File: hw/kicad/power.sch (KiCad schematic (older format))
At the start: 56 parts

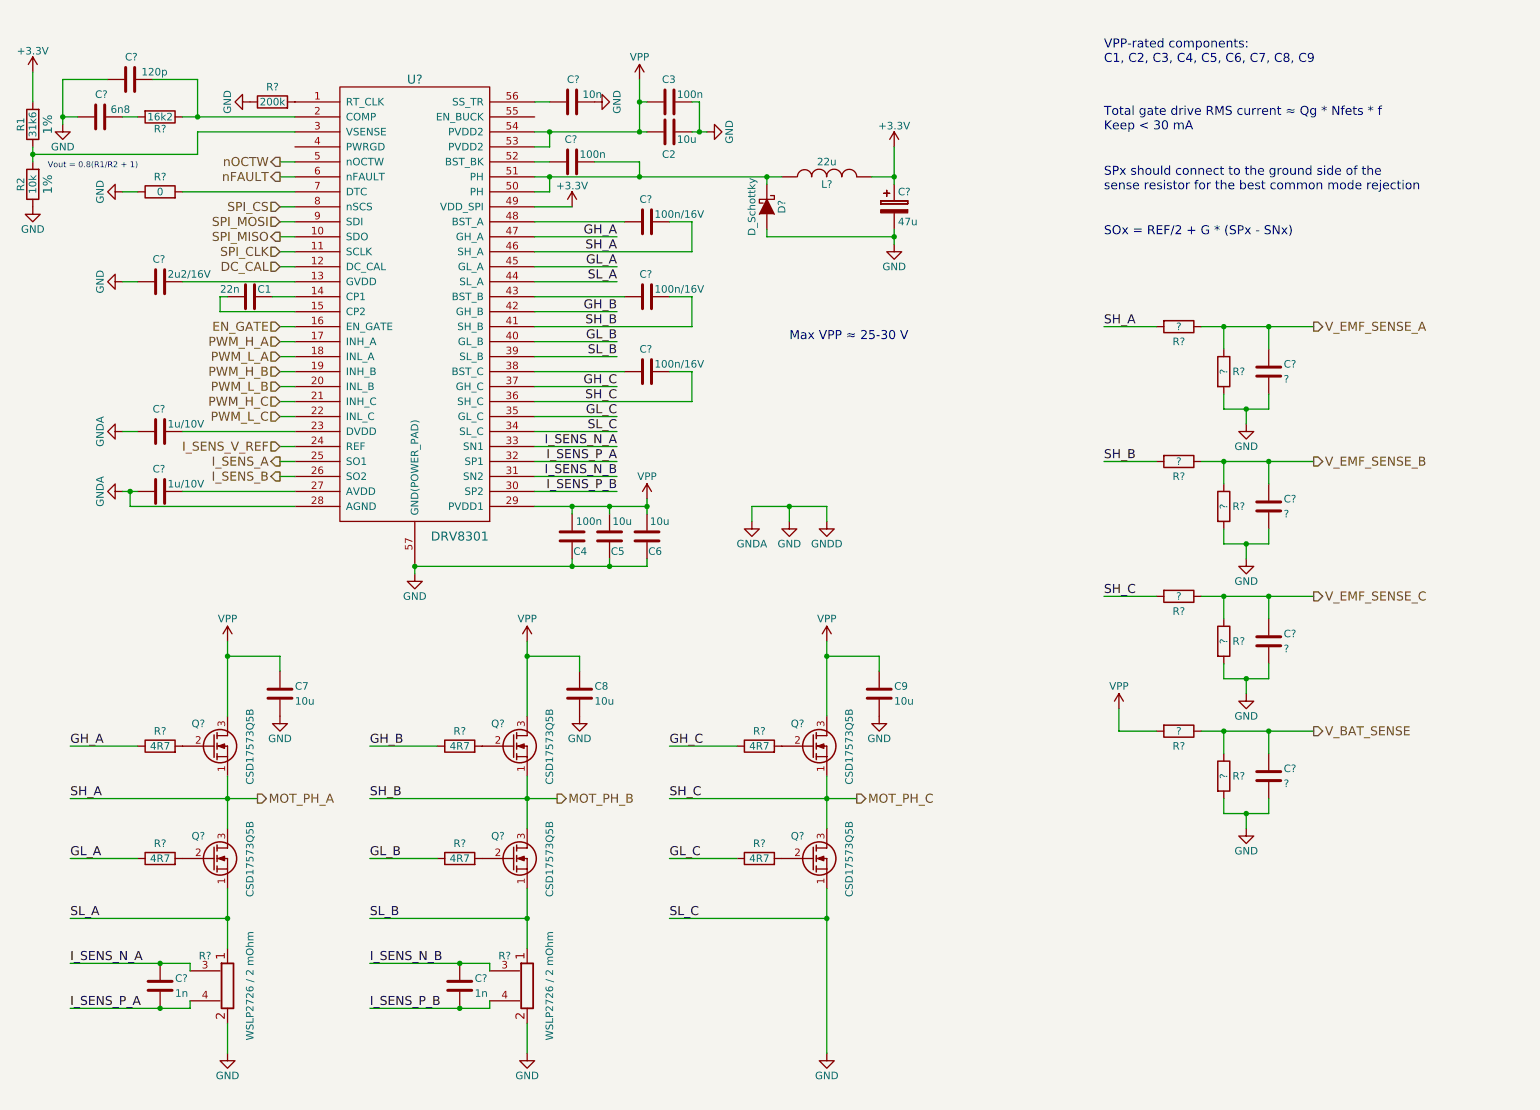
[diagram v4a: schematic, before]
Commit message: Connect mcu to drv8301
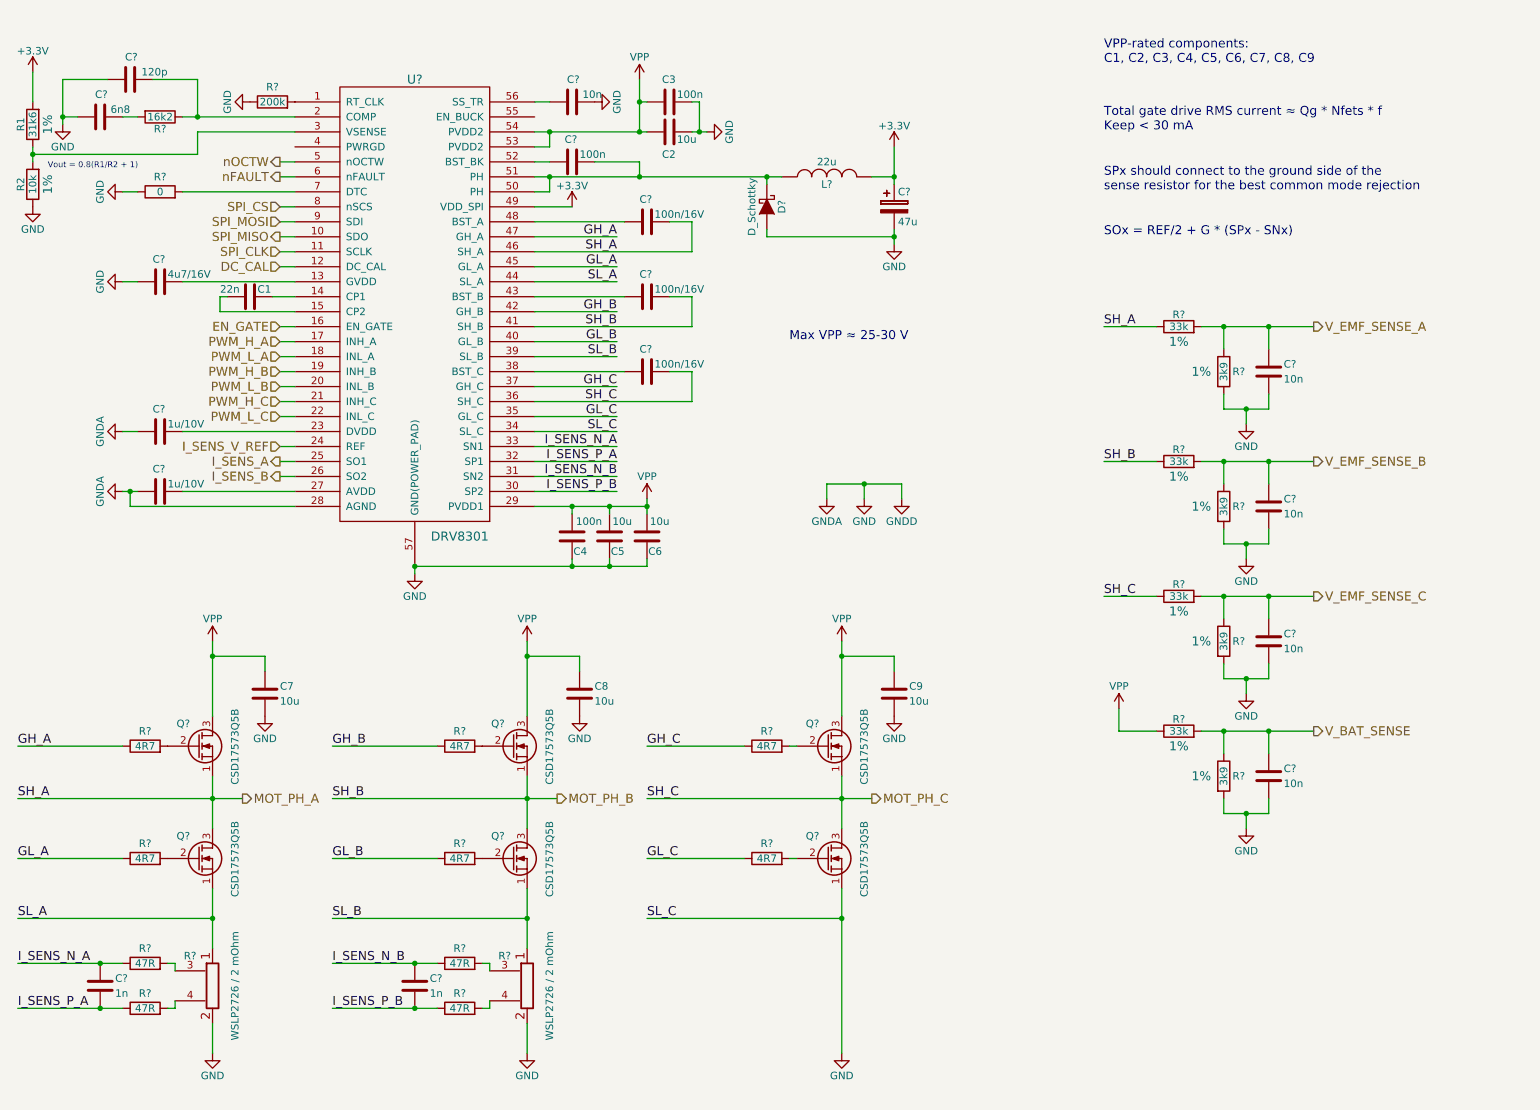
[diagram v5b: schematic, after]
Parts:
- removed C? (x3): ?, symbol C
- removed R? (x8): ?, symbol R
- removed R?: WSLP2726 / 2 mOhm, symbol WSLP2726
- added C? (x3): 10n, symbol C
- added R?: WSLP2726 / 2 mOhm, WSLP2726:WSLP2726, symbol WSLP2726
- added R? (x4): 33k, symbol R
- added R? (x4): 3k9, symbol R
- added R? (x4): 47R, symbol R
- C?: value 2u2/16V -> 4u7/16V
- C?: value ? -> 10n
- R?: footprint (none) -> WSLP2726:WSLP2726
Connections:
- net GND: now also C?.2, C?.2, C?.2, R?.2, R?.2, R?.2, R?.2, R?.2
- net I_SENS_N_A: now also R?.1; no longer R?.3
- net I_SENS_N_B: now also R?.1
- net I_SENS_P_A: now also R?.1; no longer R?.4
- net I_SENS_P_B: now also R?.1
- net MOT_PH_A: now also R?.1
- net MOT_PH_B: now also R?.1
- net MOT_PH_C: now also R?.1
- net SL_B: now also R?.1
- net VPP: now also R?.1
- net V_BAT_SENSE: now also C?.1, R?.1, R?.2
- net V_EMF_SENSE_A: now also R?.1, R?.2
- net V_EMF_SENSE_B: now also C?.1, R?.1, R?.2
- net V_EMF_SENSE_C: now also C?.1, R?.1, R?.2
- new net: R?.2, R?.3 (x2)
- new net: R?.2, R?.4 (x2)
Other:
- moved on the sheet: C7, C9, C?, Q?, R?

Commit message: Added LDO for mcu
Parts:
- R1: value 31k6 -> 36k
- R2: value 10k -> 6k8
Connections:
- net +3V3: no longer C?.1, L?.2, R1.2
- new net +5V: C?.1, L?.2, R1.2
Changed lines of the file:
@@
 LIBS:wslp2726
 LIBS:test
+LIBS:az1117c
 LIBS:MotCtrl-cache
 EELAYER 25 0
@@
 P 900 1650
 F 0 "R2" V 980 1650 50  0000 C CNN
-F 1 "10k" V 900 1650 50  0000 C CNN
+F 1 "6k8" V 900 1650 50  0000 C CNN
 F 2 "" V 830 1650 30  0000 C CNN
 F 3 "" H 900 1650 30  0000 C CNN
@@
 P 900 1250
 F 0 "R1" V 980 1250 50  0000 C CNN
-F 1 "31k6" V 900 1250 50  0000 C CNN
+F 1 "36k" V 900 1250 50  0000 C CNN
 F 2 "" V 830 1250 30  0000 C CNN
 F 3 "" H 900 1250 30  0000 C CNN
@@
 F 3 "" H 1100 1250 60  0000 C CNN
 	1    1100 1250
-	1    0    0    -1
-$EndComp
-$Comp
-L +3.3V #PWR?
-U 1 1 5815E769
-P 6650 1400
-F 0 "#PWR?" H 6650 1250 50  0001 C CNN
-F 1 "+3.3V" H 6650 1540 50  0000 C CNN
-F 2 "" H 6650 1400 60  0000 C CNN
-F 3 "" H 6650 1400 60  0000 C CNN
-	1    6650 1400
-	1    0    0    -1
-$EndComp
-$Comp
-L +3.3V #PWR?
-U 1 1 5815E7DD
-P 900 900
-F 0 "#PWR?" H 900 750 50  0001 C CNN
-F 1 "+3.3V" H 900 1040 50  0000 C CNN
-F 2 "" H 900 900 60  0000 C CNN
-F 3 "" H 900 900 60  0000 C CNN
-	1    900  900
 	1    0    0    -1
 $EndComp
@@
 	1    0    0    -1
 $EndComp
+$Comp
+L +5V #PWR?
+U 1 1 5823932E
+P 6650 1400
+F 0 "#PWR?" H 6650 1250 50  0001 C CNN
+F 1 "+5V" H 6650 1540 50  0000 C CNN
+F 2 "" H 6650 1400 60  0000 C CNN
+F 3 "" H 6650 1400 60  0000 C CNN
+	1    6650 1400
+	1    0    0    -1
+$EndComp
+$Comp
+L +5V #PWR?
+U 1 1 58239A98
+P 900 900
+F 0 "#PWR?" H 900 750 50  0001 C CNN
+F 1 "+5V" H 900 1040 50  0000 C CNN
+F 2 "" H 900 900 60  0000 C CNN
+F 3 "" H 900 900 60  0000 C CNN
+	1    900  900
+	1    0    0    -1
+$EndComp

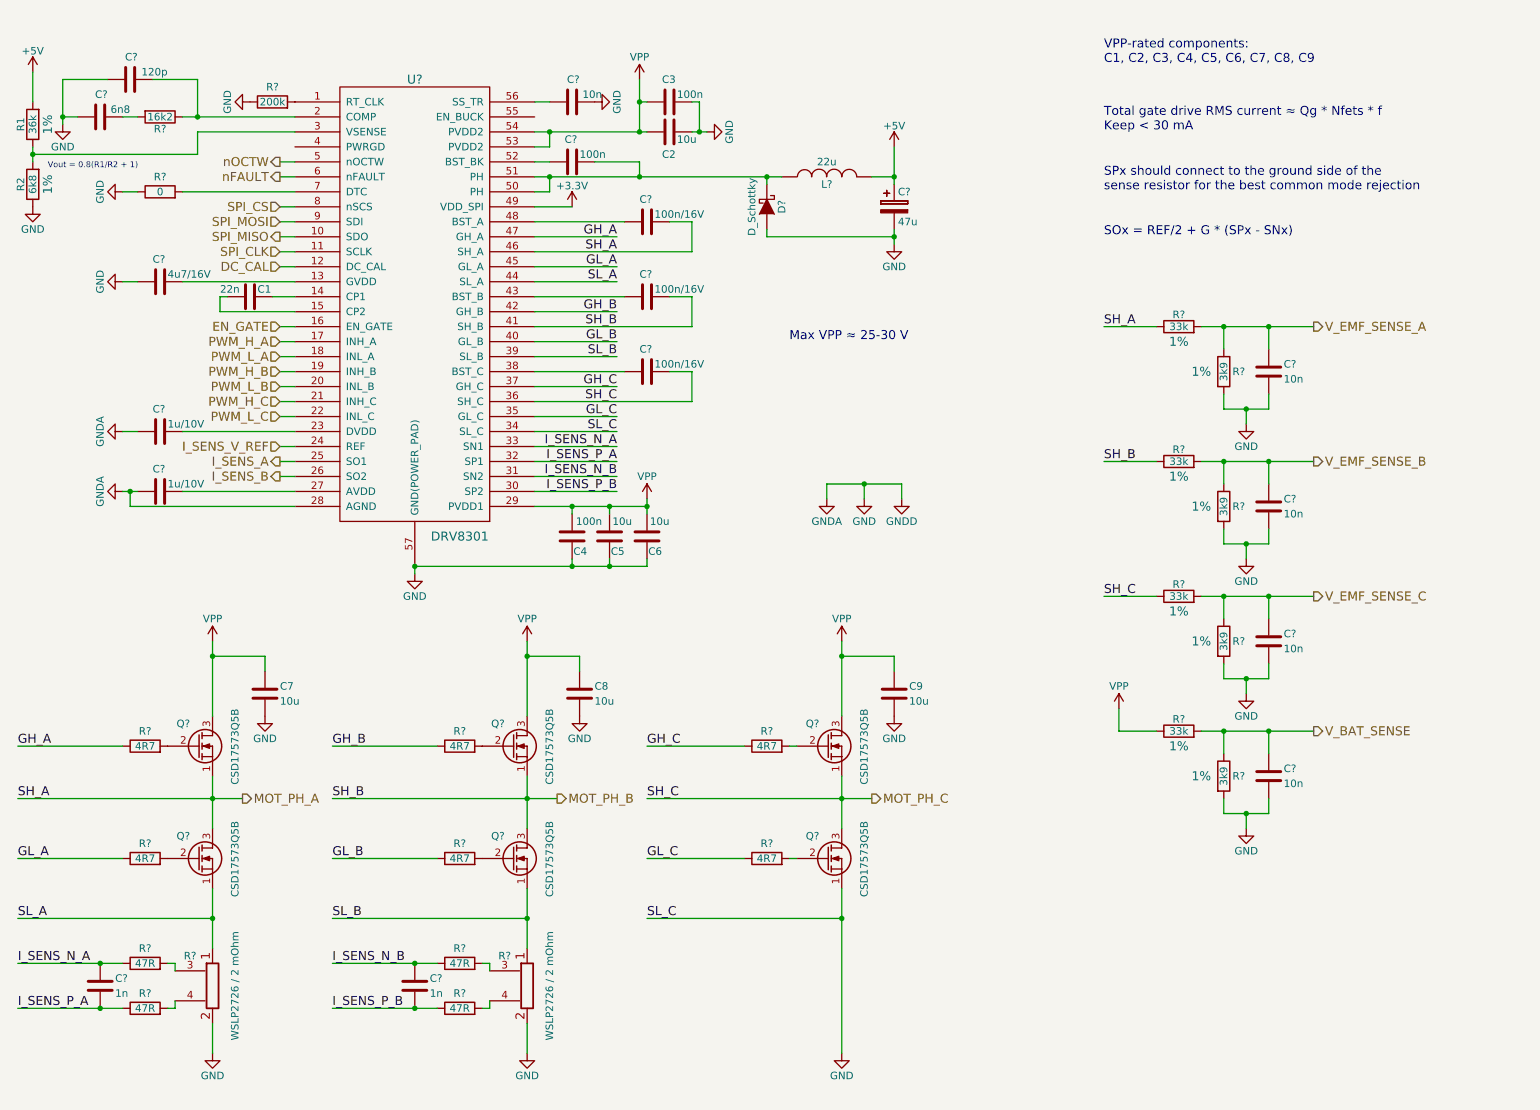
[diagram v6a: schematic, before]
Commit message: Big changes in power: new mosfets, drivers and current sensing
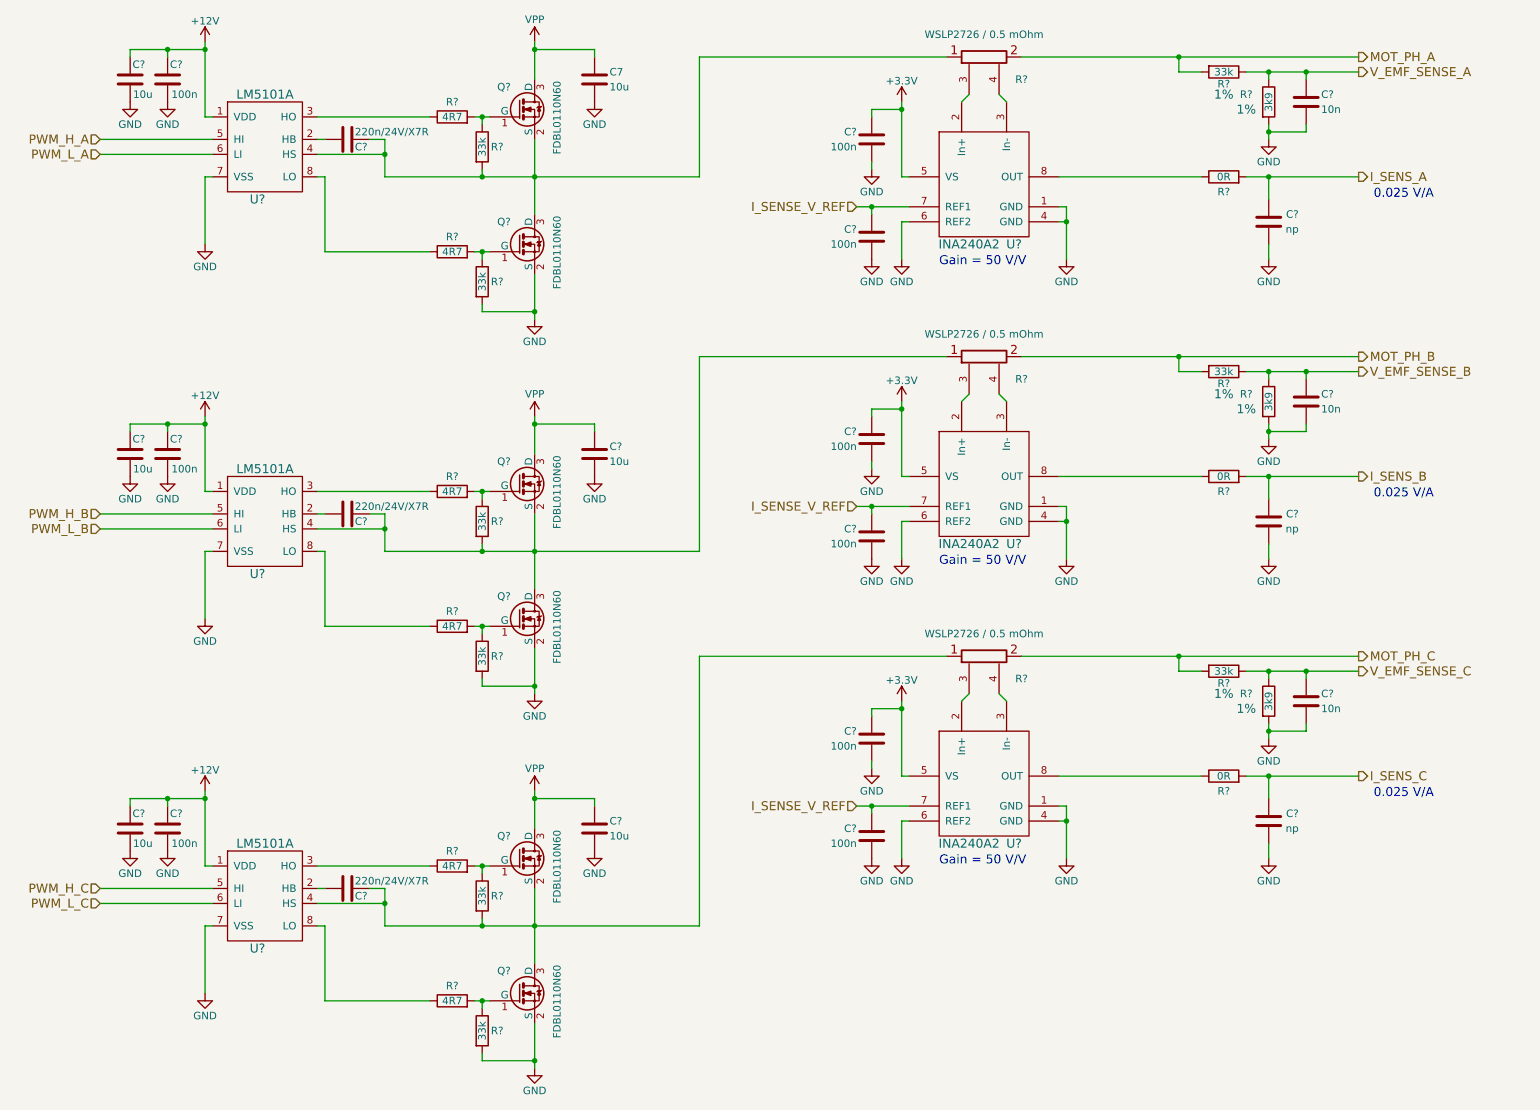
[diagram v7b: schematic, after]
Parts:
- removed C1: 22n, symbol C
- removed C2, C5, C6, C8, C9: 10u, symbol C
- removed C3, C4, C?: 100n, symbol C
- removed C? (x5): 10n, symbol C
- removed C?: 47u, symbol CP
- removed C?: 120p, symbol C
- removed C?: 6n8, symbol C
- removed C?: 4u7/16V, symbol C
- removed C? (x2): 1u/10V, symbol C
- removed C? (x3): 100n/16V, symbol C
- removed C? (x2): 1n, symbol C
- removed D?: D_Schottky, symbol D_Schottky
- removed L?: 22u, symbol INDUCTOR
- removed Q? (x6): CSD17573Q5B, SON_8_5x6:SON_8_5x6, symbol Q_NMOS_SGD
- removed R1: 36k, symbol R
- removed R2: 6k8, symbol R
- removed R?: 200k, symbol R
- removed R?: 16k2, symbol R
- removed R?: 0, symbol R
- removed R? (x4): 4R7, symbol R
- removed R?: WSLP2726 / 2 mOhm, WSLP2726:WSLP2726, symbol WSLP2726
- removed R? (x4): 33k, symbol R
- removed R? (x4): 3k9, symbol R
- removed R? (x4): 47R, symbol R
- removed U?: DRV8301, footprints:TSSOP-56-PP, symbol DRV8301
- added C? (x9): 100n, symbol C
- added C? (x3): np, symbol C
- added C? (x3): 10n, symbol C
- added C? (x3): 220n/24V/X7R, symbol C
- added C? (x5): 10u, symbol C
- added Q? (x6): FDBL0110N60, MO-299A:MO-299A, symbol FDBL0110N60
- added R? (x3): 0R, symbol R
- added R? (x9): 33k, symbol R
- added R? (x3): 3k9, symbol R
- added R? (x2): WSLP2726 / 0.5 mOhm, WSLP2726:WSLP2726, symbol WSLP2726
- added R? (x4): 4R7, symbol R
- added U? (x3): INA240A2, symbol INA240
- added U? (x3): LM5101A, symbol LM5101A
- R?: value WSLP2726 / 2 mOhm -> WSLP2726 / 0.5 mOhm
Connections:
- net +3V3: now also C?.2, C?.2, C?.2, U?.5 (VS), U?.5 (VS), U?.5 (VS)
- net GND: now also C?.1, C?.1, C?.1, C?.1, C?.1, C?.1, C?.1, C?.1, C?.1, C?.1, C?.1, C?.1, C?.1, C?.1, C?.1, C?.2, C?.2, C?.2, C?.2, C?.2, Q?.2 (S), Q?.2 (S), Q?.2 (S), R?.2, R?.2, R?.2, R?.2, R?.2, R?.2, U?.1 (GND), U?.1 (GND), U?.1 (GND), U?.4 (GND), U?.4 (GND), U?.4 (GND), U?.6 (REF2), U?.6 (REF2), U?.6 (REF2), U?.7 (VSS), U?.7 (VSS), U?.7 (VSS); no longer R?.2
- net I_SENS_A: now also C?.2, R?.2
- net I_SENS_B: now also C?.2, R?.2
- net MOT_PH_A: now also R?.2, R?.2
- net MOT_PH_B: now also R?.2, R?.2
- net MOT_PH_C: now also R?.2, R?.2
- net PWM_H_A: now also U?.5 (HI)
- net PWM_H_B: now also U?.5 (HI)
- net PWM_H_C: now also U?.5 (HI)
- net PWM_L_A: now also U?.6 (LI)
- net PWM_L_B: now also U?.6 (LI)
- net PWM_L_C: now also U?.6 (LI)
- net VPP: now also C?.1, C?.1, Q?.3 (D), Q?.3 (D), Q?.3 (D)
- net V_EMF_SENSE_A: now also C?.1, R?.1, R?.1
- net V_EMF_SENSE_B: now also C?.1, R?.1, R?.1
- net V_EMF_SENSE_C: now also C?.1, R?.1, R?.1
- net at R?.2: now also Q?.1 (G), R?.1 (x2)
- net at R?.3: now also U?.2 (In+)
- net at R?.4: now also U?.3 (In-)
- net GH_A: no longer names the net of R?.1
- net GH_A: now also U?.3 (HO)
- net GL_A: no longer names the net of R?.1
- net GL_A: now also U?.8 (LO)
- net SL_A: no longer names the net of R?.1
- net SL_A: now also C?.1, Q?.2 (S), Q?.3 (D), R?.2, U?.4 (HS)
- new net: R?.1, U?.8 (OUT) (x3)
- new net: C?.1, Q?.2 (S), Q?.3 (D), R?.1, R?.2, U?.4 (HS) (x2)
- new net: R?.3, U?.2 (In+) (x2)
- new net: R?.4, U?.3 (In-) (x2)
- new net: C?.2, U?.2 (HB) (x3)
- new net: R?.1, U?.8 (LO) (x2)
- new net: Q?.1 (G), R?.1, R?.2 (x4)
- new net: R?.1, U?.3 (HO) (x2)
- new net +12V: C?.2, C?.2, C?.2, C?.2, C?.2, C?.2, U?.1 (VDD), U?.1 (VDD), U?.1 (VDD)
- new net I_SENSE_V_REF: C?.2, C?.2, C?.2, U?.7 (REF1), U?.7 (REF1), U?.7 (REF1)
- new net I_SENS_C: C?.2, R?.2
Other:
- note added: "0.025 V/A"
- note added: "Gain = 50 V/V"
- note removed: "Max VPP ≈ 25-30 V"
- note removed: "SOx = REF/2 + G * (SPx - SNx)"
- note removed: "SPx should connect to the ground side of the \nsense resistor for the best common mode rejection"
- note removed: "Total gate drive RMS current ≈ Qg * Nfets * f\nKeep < 30 mA"
- note removed: "VPP-rated components:\nC1, C2, C3, C4, C5, C6, C7, C8, C9"
- note removed: "Vout = 0.8(R1/R2 + 1)"
- moved on the sheet: C7, R?

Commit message: Started working on power supplies
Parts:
- removed U? (x2): LM5101A, symbol LM5101A
- added U? (x2): LM5101A, WSON-8:WSON-8, symbol LM5101A
- U?: footprint (none) -> WSON-8:WSON-8
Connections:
- net +12V: now also U?.1 (VDD), U?.1 (VDD)
- net GND: now also U?.7 (VSS), U?.7 (VSS)
- net PWM_H_B: now also U?.5 (HI)
- net PWM_H_C: now also U?.5 (HI)
- net PWM_L_B: now also U?.6 (LI)
- net PWM_L_C: now also U?.6 (LI)
- net at C?.1, Q?.2 (S), Q?.3 (D)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: now also U?.4 (HS) (x2)
- net at R?.1: now also U?.8 (LO) (x2)
- net at R?.1: now also U?.3 (HO) (x2)
- net at C?.2: now also U?.2 (HB) (x2)
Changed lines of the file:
@@
 LIBS:FDBL0110N60
 LIBS:lm5101a
+LIBS:LM22675
 LIBS:MotCtrl-cache
 EELAYER 25 0
@@
 $Descr A4 11693 8268
 encoding utf-8
-Sheet 3 3
+Sheet 3 4
 Title ""
 Date ""
@@
 F 0 "U?" H 2400 1050 60  0000 C CNN
 F 1 "LM5101A" H 2450 1750 60  0000 C CNN
-F 2 "" H 2450 1400 60  0001 C CNN
+F 2 "WSON-8:WSON-8" H 2450 1400 60  0001 C CNN
 F 3 "" H 2450 1400 60  0001 C CNN
 	1    2450 1400
@@
 $EndComp
 $Comp
-L LM5101A U?
-U 1 1 5828CCE7
-P 2450 3900
-F 0 "U?" H 2400 3550 60  0000 C CNN
-F 1 "LM5101A" H 2450 4250 60  0000 C CNN
-F 2 "" H 2450 3900 60  0001 C CNN
-F 3 "" H 2450 3900 60  0001 C CNN
-	1    2450 3900
-	1    0    0    -1
-$EndComp
-$Comp
 L C C?
 U 1 1 5828CCEE
@@
 F 3 "" H 4150 7050 50  0000 L CNN
 	1    4150 7050
-	1    0    0    -1
-$EndComp
-$Comp
-L LM5101A U?
-U 1 1 5828DE11
-P 2450 6400
-F 0 "U?" H 2400 6050 60  0000 C CNN
-F 1 "LM5101A" H 2450 6750 60  0000 C CNN
-F 2 "" H 2450 6400 60  0001 C CNN
-F 3 "" H 2450 6400 60  0001 C CNN
-	1    2450 6400
 	1    0    0    -1
 $EndComp
@@
 Text Notes 9850 5750 0    60   ~ 0
 0.025 V/A
+$Comp
+L LM5101A U?
+U 1 1 582A9D5B
+P 2450 3900
+F 0 "U?" H 2400 3550 60  0000 C CNN
+F 1 "LM5101A" H 2450 4250 60  0000 C CNN
+F 2 "WSON-8:WSON-8" H 2450 3900 60  0001 C CNN
+F 3 "" H 2450 3900 60  0001 C CNN
+	1    2450 3900
+	1    0    0    -1
+$EndComp
+$Comp
+L LM5101A U?
+U 1 1 582A9E37
+P 2450 6400
+F 0 "U?" H 2400 6050 60  0000 C CNN
+F 1 "LM5101A" H 2450 6750 60  0000 C CNN
+F 2 "WSON-8:WSON-8" H 2450 6400 60  0001 C CNN
+F 3 "" H 2450 6400 60  0001 C CNN
+	1    2450 6400
+	1    0    0    -1
+$EndComp
 $EndSCHEMATC
